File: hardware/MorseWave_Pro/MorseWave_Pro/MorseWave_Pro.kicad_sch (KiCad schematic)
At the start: 29 parts, among them J1 PADDLE_3.5mm, J2 KEY_OUT_3.5mm, J3 PTT_OUT_RCA, J4 SPEAKER_8R, J5 OLED_0.96_I2C, J6 PS2_KEYBOARD, Q1 BC547, U2 PC817, U3 PC817

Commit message: Fix schematic pin alignments (0 ERC errors), complete PCB layout, and export manufacturing Gerbers v2.0
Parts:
- removed A1: Arduino_Nano_v3.x, Module:Arduino_Nano, symbol Arduino_Nano_v3.x
- removed C1, C2: 10nF, Capacitor_SMD:C_0805_2012Metric, symbol C
- removed C3, C5, C7: 100nF, Capacitor_SMD:C_0805_2012Metric, symbol C
- removed C4: 47nF, Capacitor_SMD:C_0805_2012Metric, symbol C
- removed C6: 100uF, Capacitor_SMD:CP_Elec_6.3x5.4, symbol C_Polarized
- removed D1: LED_KEY, LED_THT:LED_D3.0mm, symbol LED
- removed D2: 1N4148, Diode_SMD:D_SOD-123, symbol D
- removed J1: PADDLE_3.5mm, Connector_PinHeader_2.54mm:PinHeader_1x03_P2.54mm_Vertical, symbol Conn_01x03_Pin
- removed J2: KEY_OUT_3.5mm, Connector_PinHeader_2.54mm:PinHeader_1x02_P2.54mm_Vertical, symbol Conn_01x02_Pin
- removed J3: PTT_OUT_RCA, Connector_PinHeader_2.54mm:PinHeader_1x02_P2.54mm_Vertical, symbol Conn_01x02_Pin
- removed J4: SPEAKER_8R, Connector_JST:JST_XH_B2B-XH-A_1x02_P2.50mm_Vertical, symbol Conn_01x02_Pin
- removed J5: OLED_0.96_I2C, Connector_PinHeader_2.54mm:PinHeader_1x04_P2.54mm_Vertical, symbol Conn_01x04_Pin
- removed J6: PS2_KEYBOARD, Connector_PinHeader_2.54mm:PinHeader_1x04_P2.54mm_Vertical, symbol Conn_01x04_Pin
- removed Q1: BC547, Package_TO_SOT_THT:TO-92_Inline, symbol BC547
- removed R1, R2: 1k, Resistor_SMD:R_0805_2012Metric, symbol R
- removed R3, R4, R5: 330R, Resistor_SMD:R_0805_2012Metric, symbol R
- removed R6: 470R, Resistor_SMD:R_0805_2012Metric, symbol R
- removed R7: 33R (1W), Resistor_SMD:R_1206_3216Metric, symbol R
- removed RV1: 10k (Speed), Potentiometer_THT:Potentiometer_Alps_RK09L_Single_Vertical, symbol R_Potentiometer
- removed RV2: 10k (Tone), Potentiometer_THT:Potentiometer_Alps_RK09L_Single_Vertical, symbol R_Potentiometer
- removed RV3: 10k (Volume), Potentiometer_THT:Potentiometer_Alps_RK09L_Single_Vertical, symbol R_Potentiometer
- removed U2, U3: PC817, Package_DIP:DIP-4_W7.62mm, symbol PC817
- added A1: Arduino_Nano_v3.x, Module:Arduino_Nano, symbol MCU_Module:Arduino_Nano_v3.x
- added C1, C2: 10nF, Capacitor_SMD:C_0805_2012Metric, symbol Device:C
- added C3, C5, C7: 100nF, Capacitor_SMD:C_0805_2012Metric, symbol Device:C
- added C4: 47nF, Capacitor_SMD:C_0805_2012Metric, symbol Device:C
- added C6: 100uF, Capacitor_SMD:CP_Elec_6.3x5.4, symbol Device:C_Polarized
- added D1: LED_KEY, LED_THT:LED_D3.0mm, symbol Device:LED
- added D2: 1N4148, Diode_SMD:D_SOD-123, symbol Device:D
- added J1: PADDLE_3.5mm, Connector_PinHeader_2.54mm:PinHeader_1x03_P2.54mm_Vertical, symbol Connector:Conn_01x03_Pin
- added J2: KEY_OUT_3.5mm, Connector_PinHeader_2.54mm:PinHeader_1x02_P2.54mm_Vertical, symbol Connector:Conn_01x02_Pin
- added J3: PTT_OUT_RCA, Connector_PinHeader_2.54mm:PinHeader_1x02_P2.54mm_Vertical, symbol Connector:Conn_01x02_Pin
- added J4: SPEAKER_8R, Connector_JST:JST_XH_B2B-XH-A_1x02_P2.50mm_Vertical, symbol Connector:Conn_01x02_Pin
- added J5: OLED_0.96_I2C, Connector_PinHeader_2.54mm:PinHeader_1x04_P2.54mm_Vertical, symbol Connector:Conn_01x04_Pin
- added J6: PS2_KEYBOARD, Connector_PinHeader_2.54mm:PinHeader_1x04_P2.54mm_Vertical, symbol Connector:Conn_01x04_Pin
- added Q1: BC547, Package_TO_SOT_THT:TO-92_Inline, symbol Transistor_BJT:BC547
- added R1, R2: 1k, Resistor_SMD:R_0805_2012Metric, symbol Device:R
- added R3, R4, R5: 330R, Resistor_SMD:R_0805_2012Metric, symbol Device:R
- added R6: 470R, Resistor_SMD:R_0805_2012Metric, symbol Device:R
- added R7: 33R (1W), Resistor_SMD:R_1206_3216Metric, symbol Device:R
- added RV1: 10k (Speed), Potentiometer_THT:Potentiometer_Alps_RK09L_Single_Vertical, symbol Device:R_Potentiometer
- added RV2: 10k (Tone), Potentiometer_THT:Potentiometer_Alps_RK09L_Single_Vertical, symbol Device:R_Potentiometer
- added RV3: 10k (Volume), Potentiometer_THT:Potentiometer_Alps_RK09L_Single_Vertical, symbol Device:R_Potentiometer
- added U2, U3: PC817, Package_DIP:DIP-4_W7.62mm, symbol Isolator:PC817
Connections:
- net +5V: now also A1.27 (+5V), C6.1, C7.1, J5.2 (Pin_2), J6.1 (Pin_1), R7.2, RV1.1, RV2.1
- net AUDIO_PWM: now also A1.12 (D9), R1.1
- net DAH: now also A1.6 (D3), C2.1, J1.2 (Pin_2)
- net DIT: now also A1.5 (D2), C1.1, J1.1 (Pin_1)
- net GND: now also A1.4 (GND), C1.2, C2.2, C3.2, C4.2, C5.2, C6.2, C7.2, D1.1 (K), J1.3 (Pin_3), J5.1 (Pin_1), J6.2 (Pin_2), Q1.3 (E), RV1.3, RV2.3, RV3.3, U2.2, U3.2
- net KEY_OUT_CTRL: now also A1.13 (D10), R4.1
- net LED_KEY: now also A1.16 (D13), R3.1
- net OLED_SCL: now also A1.24 (A5), J5.3 (Pin_3)
- net OLED_SDA: now also A1.23 (A4), J5.4 (Pin_4)
- net POT_SPEED: now also A1.19 (A0), RV1.2
- net POT_TONE: now also A1.20 (A1), RV2.2
- net PS2_CLK: now also A1.8 (D5), J6.4 (Pin_4)
- net PS2_DATA: now also A1.7 (D4), J6.3 (Pin_3)
- net PTT_OUT_CTRL: now also A1.14 (D11), R5.1
- new net: J3.1 (Pin_1), U3.3
- new net: J3.2 (Pin_2), U3.4
- new net: D1.2 (A), R3.2
- new net: C5.1, J4.1 (Pin_1), Q1.1 (C)
- new net: Q1.2 (B), R6.2
- new net: C3.1, R1.2, R2.1
- new net: C4.1, R2.2, RV3.1
- new net: R6.1, RV3.2
- new net: J4.2 (Pin_2), R7.1
- new net: R4.2, U2.1
- new net: D2.2 (A), J2.1 (Pin_1), U2.3
- new net: D2.1 (K), J2.2 (Pin_2), U2.4
- new net: R5.2, U3.1
- no-connect marks 0 -> 16

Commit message: feat(hardware): finalize 100% through-hole classic PCB v2.0 (100x75mm) and high-res 3D renders
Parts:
- C1, C2, C3, C4, C5, C7: footprint Capacitor_SMD:C_0805_2012Metric -> Capacitor_THT:C_Disc_D5.0mm_W2.5mm_P5.00mm
- C6: footprint Capacitor_SMD:CP_Elec_6.3x5.4 -> Capacitor_THT:CP_Radial_D6.3mm_P2.50mm
- D2: footprint Diode_SMD:D_SOD-123 -> Diode_THT:D_DO-35_SOD27_P7.62mm_Horizontal
- R1, R2, R3, R4, R5, R6: footprint Resistor_SMD:R_0805_2012Metric -> Resistor_THT:R_Axial_DIN0207_L6.3mm_D2.5mm_P7.62mm_Horizontal
- R7: footprint Resistor_SMD:R_1206_3216Metric -> Resistor_THT:R_Axial_DIN0411_L9.9mm_D3.6mm_P12.70mm_Horizontal

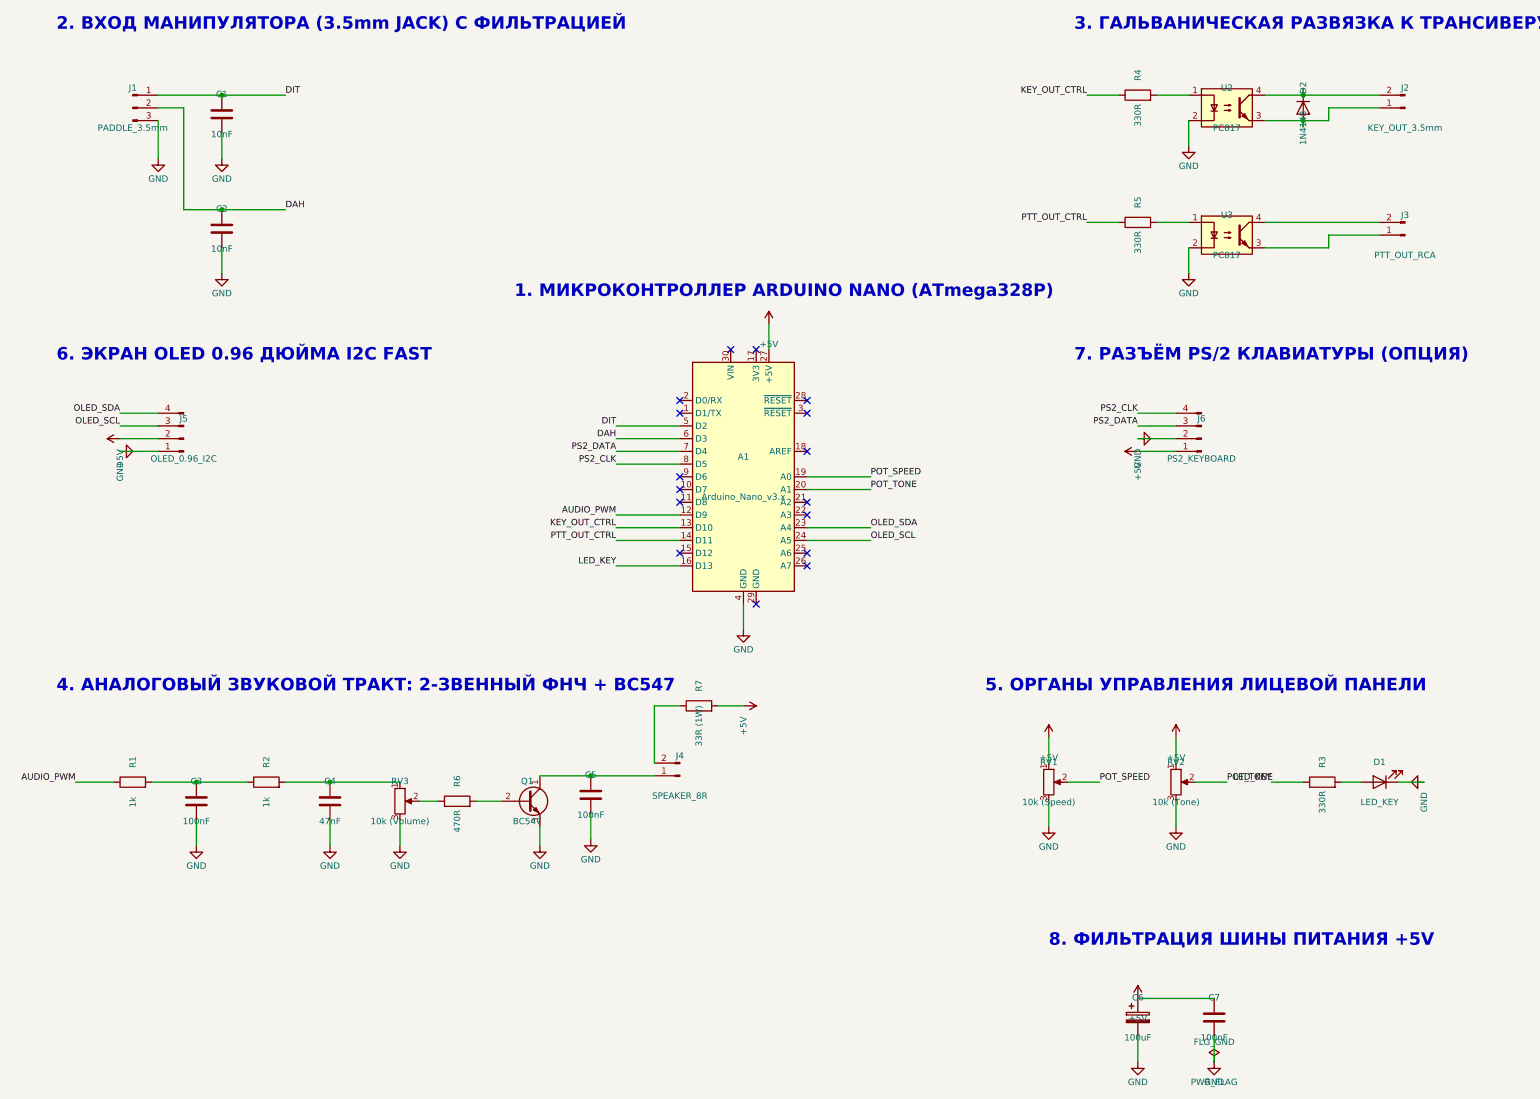
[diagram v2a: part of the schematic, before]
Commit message: feat(hardware): clean silkscreen overlaps, add telegraph key logo, By R9OGL, website, and Rezonit fab compliance
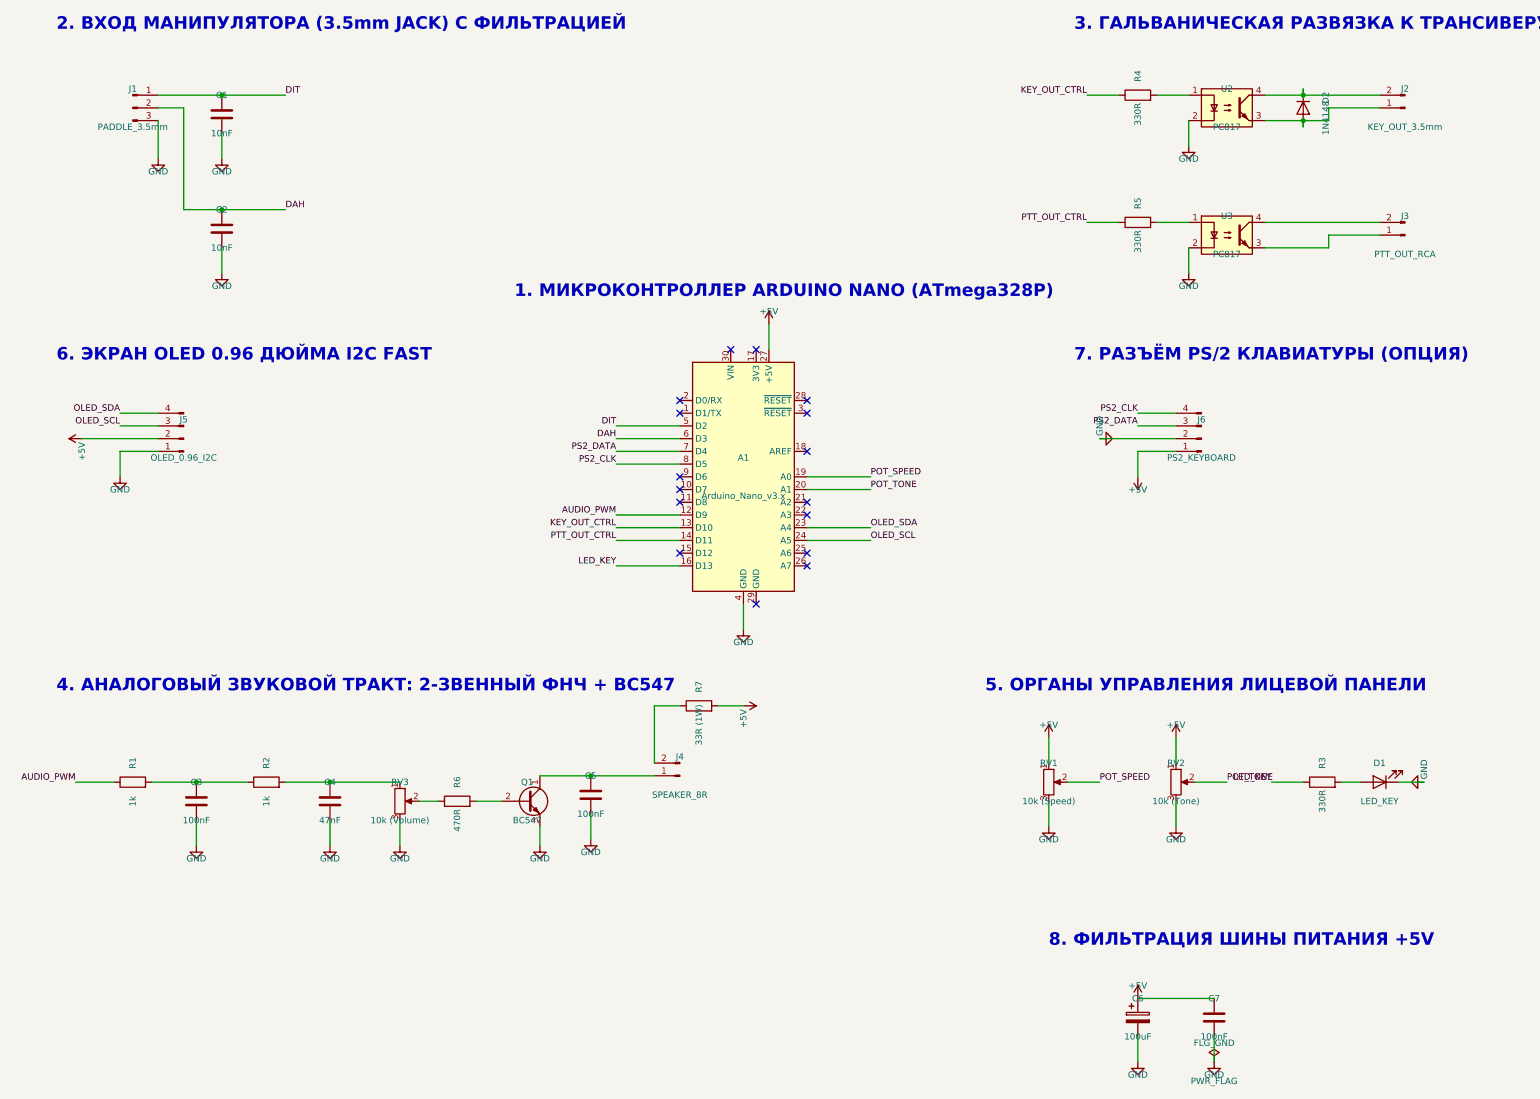
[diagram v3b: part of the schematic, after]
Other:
- company: R9OGL Hardware Workshop -> By R9OGL
- title: MorseWave Pro Keyer (R9OGL Edition) -> MorseWave Pro Keyer

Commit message: feat(hardware): finalize MorseWave Pro v2.0 THT PCB with 0 DRC errors, dedicated OLED zone, and Rezonit Gerbers
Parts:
- added J7: PHONES_3.5mm, Connector_PinHeader_2.54mm:PinHeader_1x02_P2.54mm_Vertical, symbol Connector:Conn_01x02_Pin
- added J_LED: TX_LED_WIRES, Connector_PinHeader_2.54mm:PinHeader_1x02_P2.54mm_Vertical, symbol Connector:Conn_01x02_Pin
- added J_RV1: SPEED_WIRES, Connector_PinHeader_2.54mm:PinHeader_1x03_P2.54mm_Vertical, symbol Connector:Conn_01x03_Pin
- added J_RV2: TONE_WIRES, Connector_PinHeader_2.54mm:PinHeader_1x03_P2.54mm_Vertical, symbol Connector:Conn_01x03_Pin
- added J_RV3: VOL_WIRES, Connector_PinHeader_2.54mm:PinHeader_1x03_P2.54mm_Vertical, symbol Connector:Conn_01x03_Pin
- added R8: 150R, Resistor_THT:R_Axial_DIN0207_L6.3mm_D2.5mm_P7.62mm_Horizontal, symbol Device:R
- D1: value LED_KEY -> TX_GREEN_3mm
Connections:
- net +5V: now also J_RV1.1 (Pin_1), J_RV2.1 (Pin_1)
- net AUDIO_PWM: now also A1.9 (D6); no longer A1.12 (D9)
- net GND: now also J7.2 (Pin_2), J_LED.2 (Pin_2), J_RV1.3 (Pin_3), J_RV2.3 (Pin_3), J_RV3.3 (Pin_3)
- net LED_KEY: now also A1.11 (D8); no longer A1.16 (D13)
- net POT_SPEED: now also J_RV1.2 (Pin_2)
- net POT_TONE: now also A1.21 (A2), J_RV2.2 (Pin_2); no longer A1.20 (A1)
- net at C5.1, J4.1 (Pin_1), Q1.1 (C): now also R8.1
- net at D1.2 (A), R3.2: now also J_LED.1 (Pin_1)
- net at C4.1, R2.2, RV3.1: now also J_RV3.1 (Pin_1)
- net at R6.1, RV3.2: now also J_RV3.2 (Pin_2)
- new net: J7.1 (Pin_1), R8.2
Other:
- note added: "5. ОРГАНЫ УПРАВЛЕНИЯ ЛИЦЕВОЙ ПАНЕЛИ (ПОТЕНЦИОМЕТРЫ + СВЕТОДИОД TX)"
- note removed: "5. ОРГАНЫ УПРАВЛЕНИЯ ЛИЦЕВОЙ ПАНЕЛИ"

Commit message: feat(keyer): v2.109.12 MorseWave Pro v2.0 THT board, 3D card & breadboard starter guide
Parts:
- removed J_RV1: SPEED_WIRES, Connector_PinHeader_2.54mm:PinHeader_1x03_P2.54mm_Vertical, symbol Connector:Conn_01x03_Pin
- removed J_RV2: TONE_WIRES, Connector_PinHeader_2.54mm:PinHeader_1x03_P2.54mm_Vertical, symbol Connector:Conn_01x03_Pin
- removed J_RV3: VOL_WIRES, Connector_PinHeader_2.54mm:PinHeader_1x03_P2.54mm_Vertical, symbol Connector:Conn_01x03_Pin
- added D3: PWR_GREEN_3mm, LED_THT:LED_D3.0mm, symbol Device:LED
- added J_PWR: EXT_PWR_LED, Connector_PinHeader_2.54mm:PinHeader_1x02_P2.54mm_Vertical, symbol Connector:Conn_01x02_Pin
- added R9: 1k, Resistor_THT:R_Axial_DIN0207_L6.3mm_D2.5mm_P7.62mm_Horizontal, symbol Device:R
- D1: value TX_GREEN_3mm -> KEY_RED_3mm
- J4: footprint Connector_JST:JST_XH_B2B-XH-A_1x02_P2.50mm_Vertical -> Connector_PinHeader_2.54mm:PinHeader_1x02_P2.54mm_Vertical
- J5: footprint Connector_PinHeader_2.54mm:PinHeader_1x04_P2.54mm_Vertical -> Connector_PinSocket_2.54mm:PinSocket_1x04_P2.54mm_Vertical
- J_LED: value TX_LED_WIRES -> EXT_KEY_LED
- RV1: value 10k (Speed) -> SPEED (10k); footprint Potentiometer_THT:Potentiometer_Alps_RK09L_Single_Vertical -> Connector_PinHeader_2.54mm:PinHeader_1x03_P2.54mm_Vertical
- RV2: value 10k (Tone) -> TONE (10k); footprint Potentiometer_THT:Potentiometer_Alps_RK09L_Single_Vertical -> Connector_PinHeader_2.54mm:PinHeader_1x03_P2.54mm_Vertical
- RV3: value 10k (Volume) -> VOLUME (10k); footprint Potentiometer_THT:Potentiometer_Alps_RK09L_Single_Vertical -> Connector_PinHeader_2.54mm:PinHeader_1x03_P2.54mm_Vertical
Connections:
- net +5V: now also R9.1
- net GND: now also D3.1 (K), J_PWR.2 (Pin_2)
- new net: D3.2 (A), J_PWR.1 (Pin_1), R9.2
